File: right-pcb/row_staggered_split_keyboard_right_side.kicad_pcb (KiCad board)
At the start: 2 copper layers, 165 x 132 mm, 177 parts, among them J1 Conn_01x02, SW1 SW_SPST, SW10 SW_SPST, SW11 SW_SPST, SW12 SW_SPST, SW13 SW_SPST, SW14 SW_SPST, SW15 SW_SPST, SW16 SW_SPST, SW17 SW_SPST, SW18 SW_SPST, SW19 SW_SPST, SW2 SW_SPST, SW20 SW_SPST, SW21 SW_SPST, SW22 SW_SPST, SW23 SW_SPST, SW24 SW_SPST, SW25 SW_SPST, SW26 SW_SPST, SW27 SW_SPST, SW28 SW_SPST, SW29 SW_SPST, SW3 SW_SPST, SW30 SW_SPST, SW31 SW_SPST, SW32 SW_SPST, SW33 SW_SPST, SW34 SW_SPST, SW35 SW_SPST, SW36 SW_SPST, SW37 SW_SPST, SW38 SW_SPST, SW39 SW_SPST, SW4 SW_SPST, SW40 SW_SPST, SW41 SW_SPST, SW5 SW_SPST, SW6 SW_SPST, SW7 SW_SPST, SW8 SW_SPST, SW9 SW_SPST, U1 SN74LVC1T45DBV

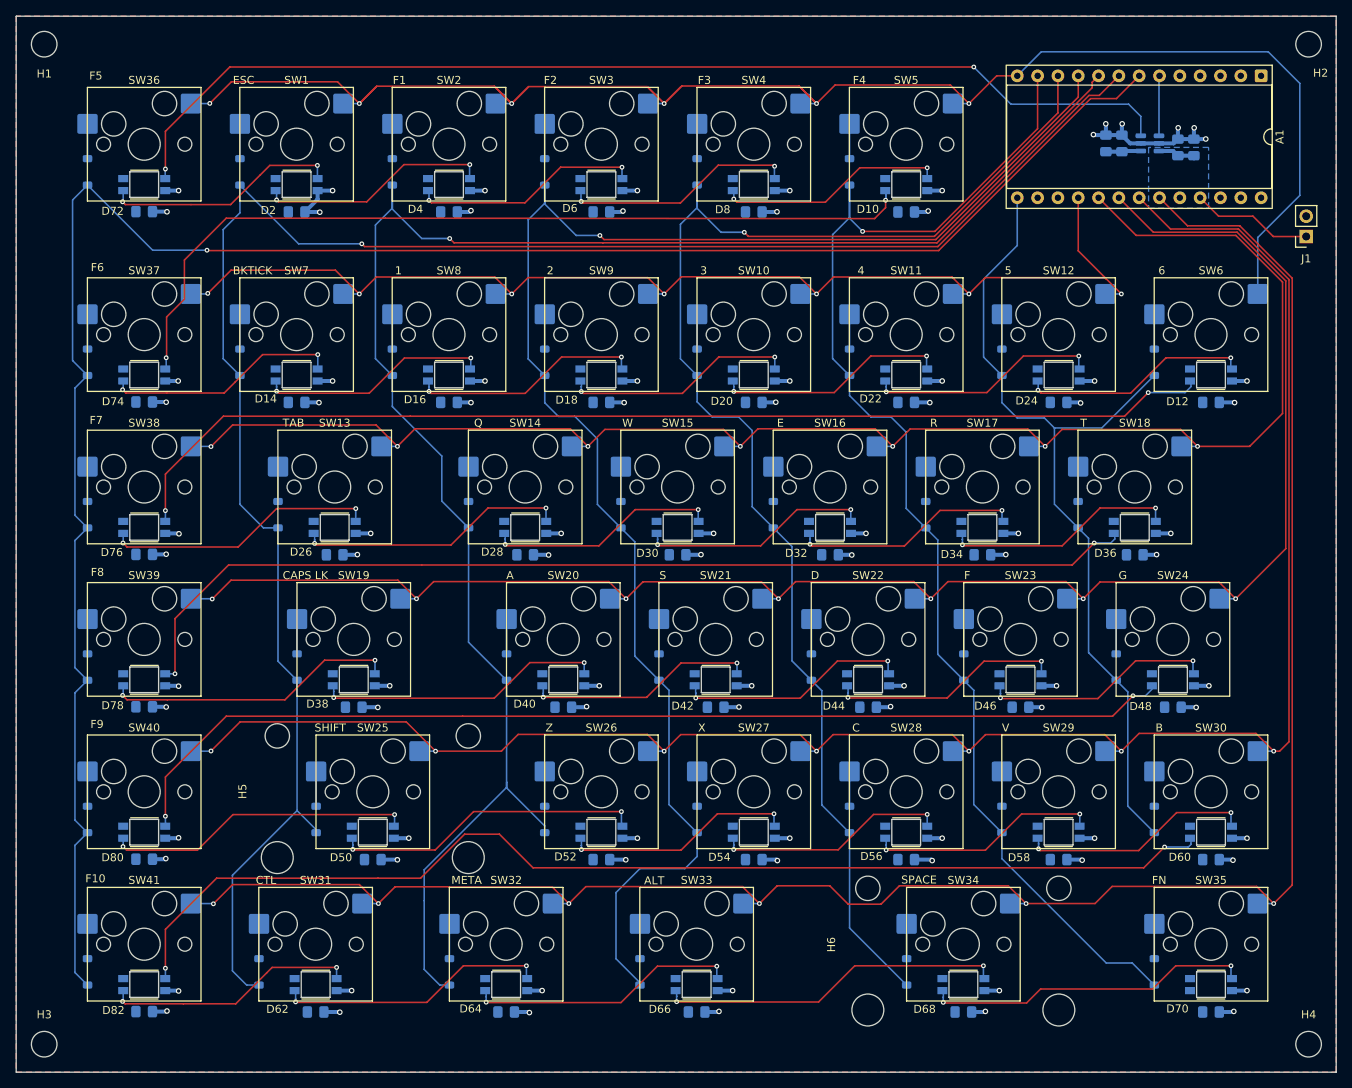
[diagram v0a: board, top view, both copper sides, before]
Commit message: initial placement of switches and modifications from left to right
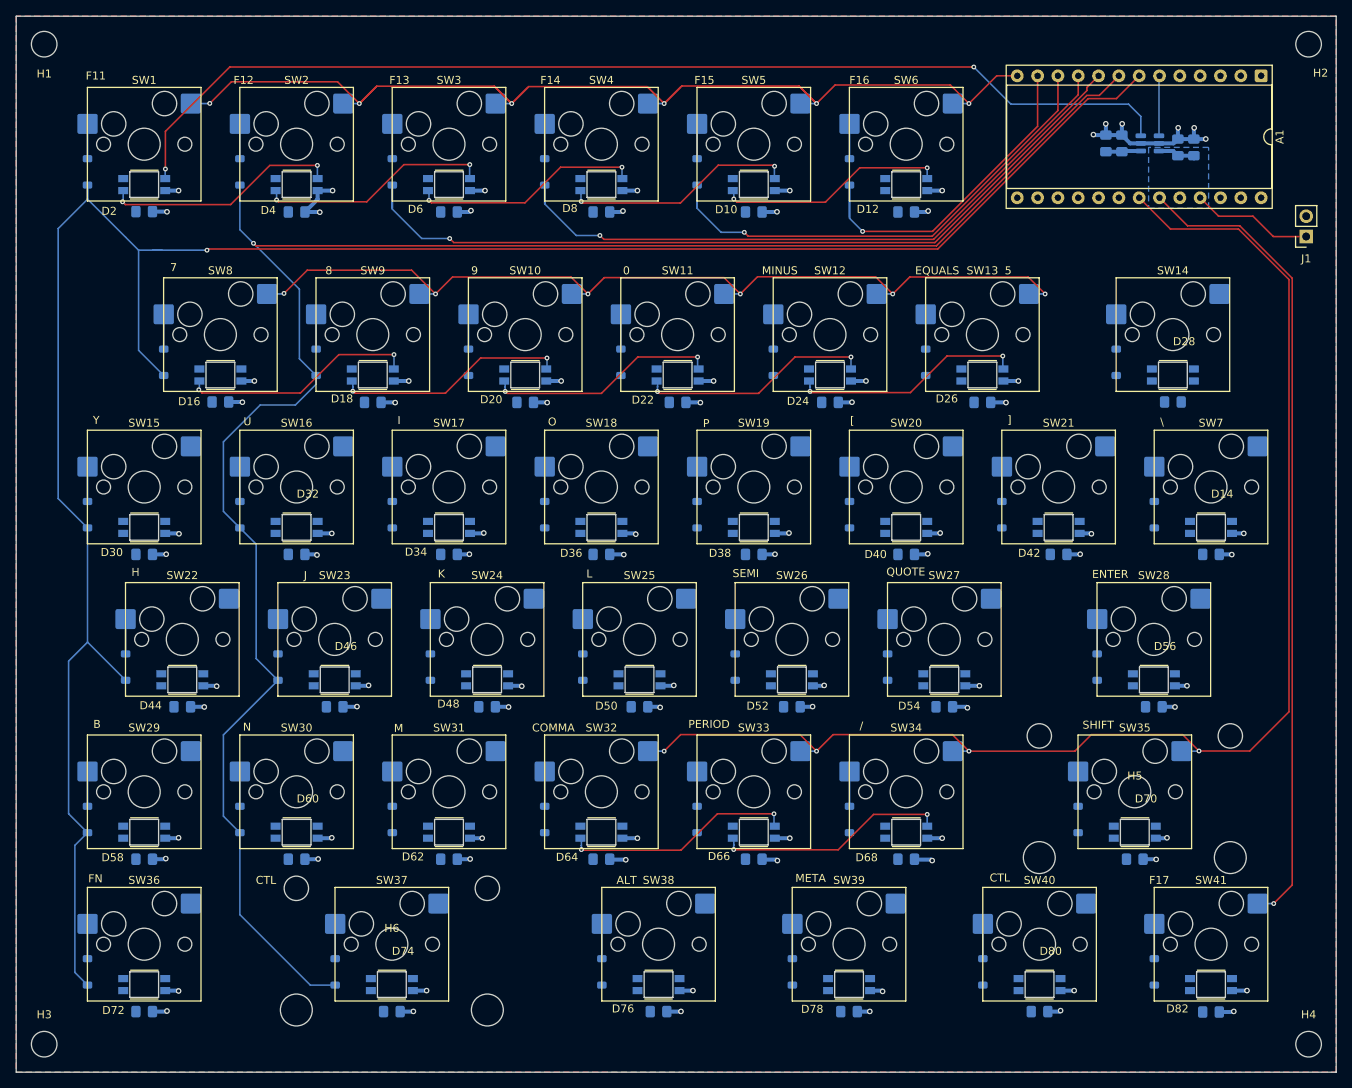
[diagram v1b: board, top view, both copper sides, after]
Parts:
- removed the C10 at (174.9, 76.8)
- removed the C16 at (155.8, 76.8)
- removed the C17 at (65.3, 95.9)
- removed the C23 at (67.7, 115.0)
- removed the C28 at (170.1, 115.0)
- removed the C29 at (70.1, 134.0)
- removed the C35 at (63.0, 153.1)
- removed the C38 at (143.9, 153.1)
- removed the D11 at (167.8, 71.8)
- removed the D12 at (174.9, 73.4)
- removed the D23 at (148.7, 71.8)
- removed the D24 at (155.8, 73.4)
- removed the D25 at (58.3, 90.9)
- removed the D26 at (65.3, 92.5)
- removed the D37 at (60.6, 109.9)
- removed the D38 at (67.7, 111.5)
- removed the D47 at (163.0, 109.9)
- removed the D48 at (170.1, 111.5)
- removed the D49 at (63.0, 129.0)
- removed the D50 at (70.1, 130.6)
- removed the D61 at (55.9, 148.0)
- removed the D62 at (63.0, 149.6)
- removed the D67 at (136.8, 148.0)
- removed the D68 at (143.9, 149.6)
- removed the SW12 at (155.8, 68.4)
- removed the SW13 at (65.3, 87.4)
- removed the SW19 at (67.7, 106.5)
- removed the SW24 at (170.1, 106.5)
- removed the SW25 at (70.1, 125.5)
- removed the SW31 at (63.0, 144.6)
- removed the SW34 at (143.9, 144.6)
- removed the SW6 at (174.9, 68.4)
- added C11: 100nF, Capacitor_SMD:C_0805_2012Metric_Pad1.18x1.45mm_HandSolder, B.Cu at (174.9, 95.8)
- added C18: 100nF, Capacitor_SMD:C_0805_2012Metric_Pad1.18x1.45mm_HandSolder, B.Cu at (170.1, 76.8)
- added C20: 100nF, Capacitor_SMD:C_0805_2012Metric_Pad1.18x1.45mm_HandSolder, B.Cu at (60.6, 95.8)
- added C27: 100nF, Capacitor_SMD:C_0805_2012Metric_Pad1.18x1.45mm_HandSolder, B.Cu at (65.3, 114.9)
- added C32: 100nF, Capacitor_SMD:C_0805_2012Metric_Pad1.18x1.45mm_HandSolder, B.Cu at (167.7, 114.9)
- added C39: 100nF, Capacitor_SMD:C_0805_2012Metric_Pad1.18x1.45mm_HandSolder, B.Cu at (165.3, 133.9)
- added C41: 100nF, Capacitor_SMD:C_0805_2012Metric_Pad1.18x1.45mm_HandSolder, B.Cu at (72.5, 153.0)
- added C44: 100nF, Capacitor_SMD:C_0805_2012Metric_Pad1.18x1.45mm_HandSolder, B.Cu at (153.4, 153.0)
- added D13: 1N4148W, Diode_SMD:D_SOD-123, B.Cu at (167.8, 90.9)
- added D14: SK6812MINI-E, SW-Adafruit:LED_SK6812MINI-E_REVERSE_MOUNT_3.2x2.8mm_P1.09mm, F.Cu at (174.9, 92.5)
- added D27: 1N4148W, Diode_SMD:D_SOD-123, B.Cu at (163.0, 71.8)
- added D28: SK6812MINI-E, SW-Adafruit:LED_SK6812MINI-E_REVERSE_MOUNT_3.2x2.8mm_P1.09mm, F.Cu at (170.1, 73.4)
- added D31: 1N4148W, Diode_SMD:D_SOD-123, B.Cu at (53.5, 90.9)
- added D32: SK6812MINI-E, SW-Adafruit:LED_SK6812MINI-E_REVERSE_MOUNT_3.2x2.8mm_P1.09mm, F.Cu at (60.6, 92.5)
- added D45: 1N4148W, Diode_SMD:D_SOD-123, B.Cu at (58.3, 109.9)
- added D46: SK6812MINI-E, SW-Adafruit:LED_SK6812MINI-E_REVERSE_MOUNT_3.2x2.8mm_P1.09mm, F.Cu at (65.3, 111.5)
- added D55: 1N4148W, Diode_SMD:D_SOD-123, B.Cu at (160.6, 109.9)
- added D56: SK6812MINI-E, SW-Adafruit:LED_SK6812MINI-E_REVERSE_MOUNT_3.2x2.8mm_P1.09mm, F.Cu at (167.7, 111.5)
- added D69: 1N4148W, Diode_SMD:D_SOD-123, B.Cu at (158.3, 129.0)
- added D70: SK6812MINI-E, SW-Adafruit:LED_SK6812MINI-E_REVERSE_MOUNT_3.2x2.8mm_P1.09mm, F.Cu at (165.3, 130.6)
- added D73: 1N4148W, Diode_SMD:D_SOD-123, B.Cu at (65.4, 148.0)
- added D74: SK6812MINI-E, SW-Adafruit:LED_SK6812MINI-E_REVERSE_MOUNT_3.2x2.8mm_P1.09mm, F.Cu at (72.5, 149.6)
- added D79: 1N4148W, Diode_SMD:D_SOD-123, B.Cu at (146.4, 148.0)
- added D80: SK6812MINI-E, SW-Adafruit:LED_SK6812MINI-E_REVERSE_MOUNT_3.2x2.8mm_P1.09mm, F.Cu at (153.4, 149.6)
- added SW14: SW_SPST, PCM_Switch_Keyboard_Hotswap_Kailh:SW_Hotswap_Kailh_MX_1.50u, F.Cu at (170.1, 68.4)
- added SW16: SW_SPST, PCM_Switch_Keyboard_Hotswap_Kailh:SW_Hotswap_Kailh_MX_1.00u, F.Cu at (60.6, 87.4)
- added SW23: SW_SPST, PCM_Switch_Keyboard_Hotswap_Kailh:SW_Hotswap_Kailh_MX_1.00u, F.Cu at (65.3, 106.5)
- added SW28: SW_SPST, PCM_Switch_Keyboard_Hotswap_Kailh:SW_Hotswap_Kailh_MX_1.75u, F.Cu at (167.7, 106.5)
- added SW35: SW_SPST, PCM_Switch_Keyboard_Hotswap_Kailh:SW_Hotswap_Kailh_MX_2.00u, F.Cu at (165.3, 125.5)
- added SW37: SW_SPST, PCM_Switch_Keyboard_Hotswap_Kailh:SW_Hotswap_Kailh_MX_2.25u, F.Cu at (72.5, 144.6)
- added SW40: SW_SPST, PCM_Switch_Keyboard_Hotswap_Kailh:SW_Hotswap_Kailh_MX_1.25u, F.Cu at (153.4, 144.6)
- added SW7: SW_SPST, PCM_Switch_Keyboard_Hotswap_Kailh:SW_Hotswap_Kailh_MX_1.00u, F.Cu at (174.9, 87.4)
- moved C34 114.3 mm to (60.6, 133.9)
- moved D60 114.3 mm to (60.6, 130.6)
- moved SW30 114.3 mm to (60.6, 125.5)
- moved D59 114.3 mm to (53.5, 129.0)
- moved H5 95.2 mm to (165.3, 125.5)
- moved H6 71.4 mm to (72.5, 144.6)
- moved C36 19.1 mm to (98.7, 133.9)
- moved C42 19.1 mm to (105.8, 153.0)
- moved C43 19.1 mm to (129.6, 153.0)
- moved C35 19.1 mm to (79.6, 133.9)
- moved C37 19.1 mm to (117.7, 133.9)
- moved C38 19.1 mm to (136.8, 133.9)
- moved D64 19.0 mm to (98.7, 130.6)
- moved D65 19.0 mm to (110.6, 129.0)
- moved D76 19.0 mm to (105.8, 149.6)
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- renumbered C9 to C10, C41 to C12, C11 to C13, C12 to C14, C13 to C15, C14 to C16, C15 to C17, C42 to C19, C18 to C21, C19 to C22, C20 to C23, C21 to C24, C22 to C25, C43 to C26, C24 to C28, C25 to C29, C26 to C30, C27 to C31, C44 to C33, C30 to C35, C31 to C36, C32 to C37, C33 to C38, C45 to C40, C36 to C42, C37 to C43, C39 to C45, C40 to C5, C5 to C6, C6 to C7, C7 to C8, C8 to C9, D71 to D1, D8 to D10, D9 to D11, D10 to D12, D73 to D15, D74 to D16, D13 to D17, D14 to D18, D15 to D19, D72 to D2, D16 to D20, D17 to D21, D18 to D22, D19 to D23, D20 to D24, D21 to D25, D22 to D26, D75 to D29, D1 to D3, D76 to D30, D27 to D33, D28 to D34, D29 to D35, D30 to D36, D31 to D37, D32 to D38, D33 to D39, D2 to D4, D34 to D40, D35 to D41, D36 to D42, D77 to D43, D78 to D44, D39 to D47, D40 to D48, D41 to D49, D3 to D5, D42 to D50, D43 to D51, D44 to D52, D45 to D53, D46 to D54, D79 to D57, D80 to D58, D4 to D6, D51 to D61, D52 to D62, D53 to D63, D54 to D64, D55 to D65, D56 to D66, D57 to D67, D58 to D68, D5 to D7, D81 to D71, D82 to D72, D63 to D75, D64 to D76, D65 to D77, D66 to D78, D6 to D8, D69 to D81, D70 to D82, D7 to D9, SW36 to SW1, SW8 to SW10, SW9 to SW11, SW10 to SW12, SW11 to SW13, SW38 to SW15, SW14 to SW17, SW15 to SW18, SW16 to SW19, SW1 to SW2, SW17 to SW20, SW18 to SW21, SW39 to SW22, SW20 to SW24, SW21 to SW25, SW22 to SW26, SW23 to SW27, SW40 to SW29, SW2 to SW3, SW26 to SW31, SW27 to SW32, SW28 to SW33, SW29 to SW34, SW41 to SW36, SW32 to SW38, SW33 to SW39, SW3 to SW4, SW35 to SW41, SW4 to SW5, SW5 to SW6, SW37 to SW8, SW7 to SW9
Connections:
- A1 pad 15: unconnected-(A1-MO-Pad15) -> /COL7
- D30 pad 4: /R1C6/DOUT -> /R2C6/DOUT
- D44 pad 4: /R3C6/DOUT -> /R3C7/DOUT
- D59 pad 1: /COL6 -> /COL1
- D60 pad 2: /R5C6/DOUT -> /R5C1/DOUT
- D60 pad 4: /R5C5/DOUT -> /R5C0/DOUT
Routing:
- net /ROW4: track 220.9 -> 0.00 mm, vias 7 -> 0
- net /ROW3: track 205.1 -> 0.00 mm, vias 7 -> 0
- net /ROW6: track 256.2 -> 101.9 mm, vias 6 -> 1
- net /R5C6/DOUT: track 143.0 -> 0.00 mm, vias 2 -> 0
- net /R1C6/DOUT: track 139.3 -> 0.00 mm, vias 2 -> 0
- net /R4C6/DOUT: track 134.5 -> 0.00 mm, vias 2 -> 0
- net /R3C6/DOUT: track 130.4 -> 0.00 mm, vias 2 -> 0
- net /COL2: track 224.3 -> 104.8 mm
- net /COL3: track 200.5 -> 83.0 mm
- net /COL5: track 161.2 -> 44.2 mm
- net /COL4: track 175.0 -> 63.1 mm
- net /R1C5/DOUT: track 108.2 -> 0.00 mm, vias 2 -> 0
- net /COL6: track 107.1 -> 0.00 mm
- net /ROW5: track 242.2 -> 170.5 mm, vias 7 -> 4
- net /ROW1: track 208.7 -> 142.1 mm
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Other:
- board text added: "/"
- board text added: "0"
- board text added: "7"
- board text added: "8"
- board text added: "9"
- board text added: "COMMA"
- board text added: "ENTER"
- board text added: "EQUALS"
- board text added: "F11"
- board text added: "F12"
- board text added: "F13"
- board text added: "F14"
- board text added: "F15"
- board text added: "F16"
- board text added: "F17"
- board text added: "H"
- board text added: "I"
- board text added: "J"
- board text added: "K"
- board text added: "L"
- board text added: "M"
- board text added: "MINUS"
- board text added: "N"
- board text added: "O"
- board text added: "P"
- board text added: "PERIOD"
- board text added: "QUOTE"
- board text added: "SEMI"
- board text added: "U"
- board text added: "Y"
- board text added: "["
- board text added: "\"
- board text added: "]"
- board text removed: "1"
- board text removed: "2"
- board text removed: "3"
- board text removed: "4"
- board text removed: "6"
- board text removed: "A"
- board text removed: "BKTICK"
- board text removed: "C"
- board text removed: "CAPS LK"
- board text removed: "D"
- board text removed: "E"
- board text removed: "ESC"
- board text removed: "F"
- board text removed: "F1"
- board text removed: "F10"
- board text removed: "F2"
- board text removed: "F3"
- board text removed: "F4"
- board text removed: "F5"
- board text removed: "F6"
- board text removed: "F7"
- board text removed: "F8"
- board text removed: "F9"
- board text removed: "G"
- board text removed: "Q"
- board text removed: "R"
- board text removed: "S"
- board text removed: "SPACE"
- board text removed: "T"
- board text removed: "TAB"
- board text removed: "V"
- board text removed: "W"
- board text removed: "X"
- board text removed: "Z"

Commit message: a bunch of DRC fixes and pcb work
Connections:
- A1 pad 15: /COL7 -> unconnected-(A1-MO-Pad15)
- D75 pad 1: /COL2 -> /COL3
- D77 pad 1: /COL3 -> /COL4
- D79 pad 1: /COL4 -> /COL5
- D81 pad 1: /COL5 -> /COL6
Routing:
- net /ROW4: track 0.00 -> 217.0 mm, vias 0 -> 7
- net /ROW3: track 0.00 -> 207.1 mm, vias 0 -> 7
- net /ROW6: track 101.9 -> 256.2 mm, vias 1 -> 6
- net /R3C7/DOUT: track 0.00 -> 134.5 mm, vias 0 -> 2
- net /R2C6/DOUT: track 0.00 -> 134.5 mm, vias 0 -> 2
- net /COL6: track 0.00 -> 132.8 mm
- net /R4C6/DOUT: track 0.00 -> 131.8 mm, vias 0 -> 2
- net /R5C6/DOUT: track 0.00 -> 129.0 mm, vias 0 -> 2
- net /COL5: track 44.2 -> 167.3 mm
- net /COL4: track 63.1 -> 179.1 mm
- net /COL3: track 83.0 -> 198.9 mm
- net /R1C5/DOUT: track 0.00 -> 102.8 mm, vias 0 -> 2
- net /COL2: track 104.8 -> 196.6 mm
- net /ROW5: track 170.5 -> 239.1 mm, vias 4 -> 7
- net /ROW1: track 142.1 -> 210.4 mm
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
